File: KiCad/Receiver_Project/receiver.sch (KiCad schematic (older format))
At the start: 28 parts, among them J1 RB1-125BAG1A, U1 MC7805CTG, U2 LM7171, U3 LM7171, U4 Physical_Mount, U5 Physical_Mount

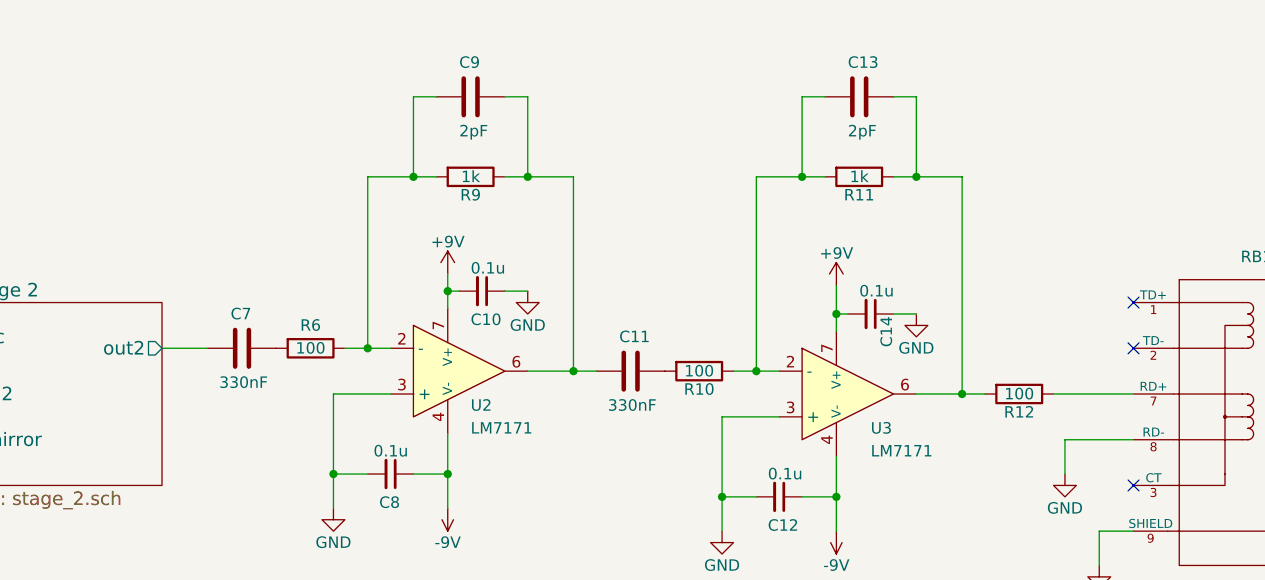
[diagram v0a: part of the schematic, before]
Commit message: added simulation labels to receiver schematic
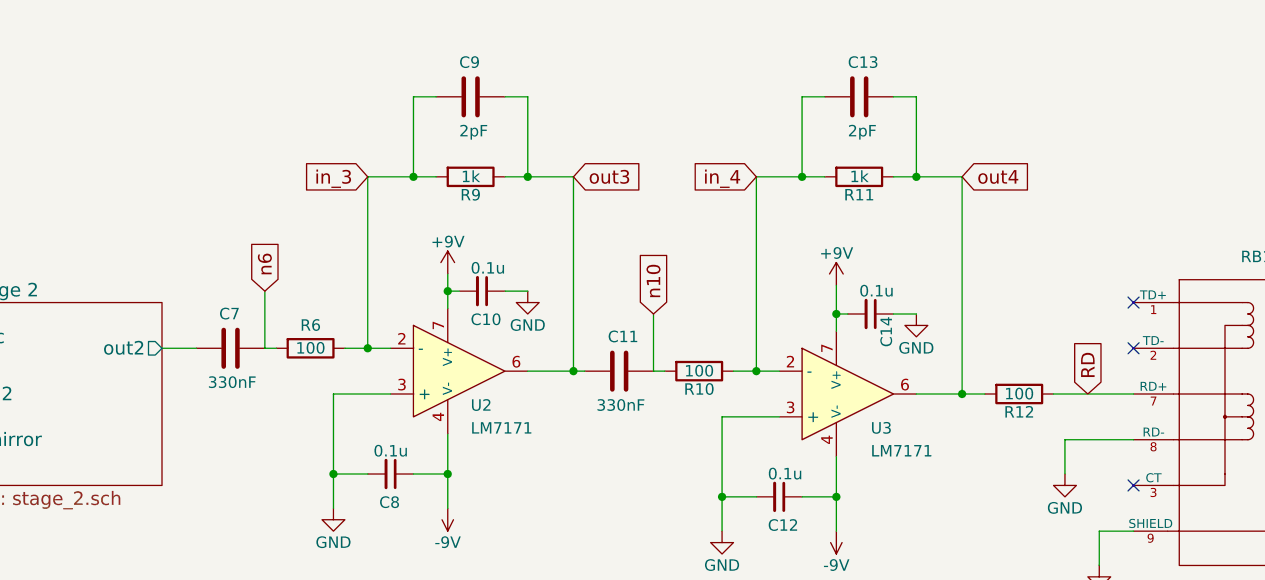
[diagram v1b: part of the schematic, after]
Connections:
- net RD: now reaches J1.7 (RD+), R12.1
- net in_3: now reaches C9.2, R6.1, R9.2, U2.2 (-)
- net out3: now reaches C11.2, C9.1, R9.1, U2.6
- net in_4: now reaches C13.2, R10.1, R11.2, U3.2 (-)
- net out4: now reaches C13.1, R11.1, R12.2, U3.6
- net n6: now reaches C7.1, R6.2
- net n10: now reaches C11.1, R10.2
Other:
- moved on the sheet: C11, C7
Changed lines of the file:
@@
 L C C7
 U 1 1 56FA0FD5
-P 5200 4000
-F 0 "C7" V 5050 3950 50  0000 L CNN
-F 1 "330nF" V 5350 3900 50  0000 L CNN
-F 2 "UC_the_Fish_Components:200Mil_Passive" H 5238 3850 50  0001 C CNN
-F 3 "" H 5200 4000 50  0000 C CNN
-	1    5200 4000
+P 5150 4000
+F 0 "C7" V 5000 3950 50  0000 L CNN
+F 1 "330nF" V 5300 3900 50  0000 L CNN
+F 2 "UC_the_Fish_Components:200Mil_Passive" H 5188 3850 50  0001 C CNN
+F 3 "" H 5150 4000 50  0000 C CNN
+	1    5150 4000
 	0    1    1    0
 $EndComp
@@
 L C C11
 U 1 1 56FA1070
-P 6900 4100
-F 0 "C11" V 6750 4050 50  0000 L CNN
-F 1 "330nF" V 7050 4000 50  0000 L CNN
-F 2 "UC_the_Fish_Components:200Mil_Passive" H 6938 3950 50  0001 C CNN
-F 3 "" H 6900 4100 50  0000 C CNN
-	1    6900 4100
+P 6850 4100
+F 0 "C11" V 6700 4050 50  0000 L CNN
+F 1 "330nF" V 7000 4000 50  0000 L CNN
+F 2 "UC_the_Fish_Components:200Mil_Passive" H 6888 3950 50  0001 C CNN
+F 3 "" H 6850 4100 50  0000 C CNN
+	1    6850 4100
 	0    1    1    0
 $EndComp
@@
 $EndComp
 Wire Wire Line
-	4850 4000 5050 4000
+	4850 4000 5000 4000
 Wire Wire Line
 	5650 4000 5850 4000
@@
 	5750 3250 6050 3250
 Wire Wire Line
-	6450 4100 6750 4100
+	6450 4100 6700 4100
 Wire Wire Line
 	6350 3250 6650 3250
@@
 	1    0    0    -1
 $EndComp
+Text GLabel 5300 3750 1    59   Input ~ 0
+n6
+Wire Wire Line
+	5300 4000 5350 4000
+Wire Wire Line
+	5300 4000 5300 3750
+Text GLabel 5750 3250 0    59   Input ~ 0
+in_3
+Text GLabel 6650 3250 2    59   Input ~ 0
+out3
+Wire Wire Line
+	7050 4100 7000 4100
+Wire Wire Line
+	7000 4100 7000 3850
+Text GLabel 7000 3850 1    59   Input ~ 0
+n10
+Text GLabel 7450 3250 0    59   Input ~ 0
+in_4
+Text GLabel 8350 3250 2    59   Input ~ 0
+out4
+Text GLabel 8900 4200 1    59   Input ~ 0
+RD
 $EndSCHEMATC
